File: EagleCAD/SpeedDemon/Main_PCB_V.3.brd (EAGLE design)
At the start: 77 x 46.5 mm, 65 parts, among them Q1 DMC2700, U3 LM3676, U4 STM32F072-LQFP48, X1 32.768kHz

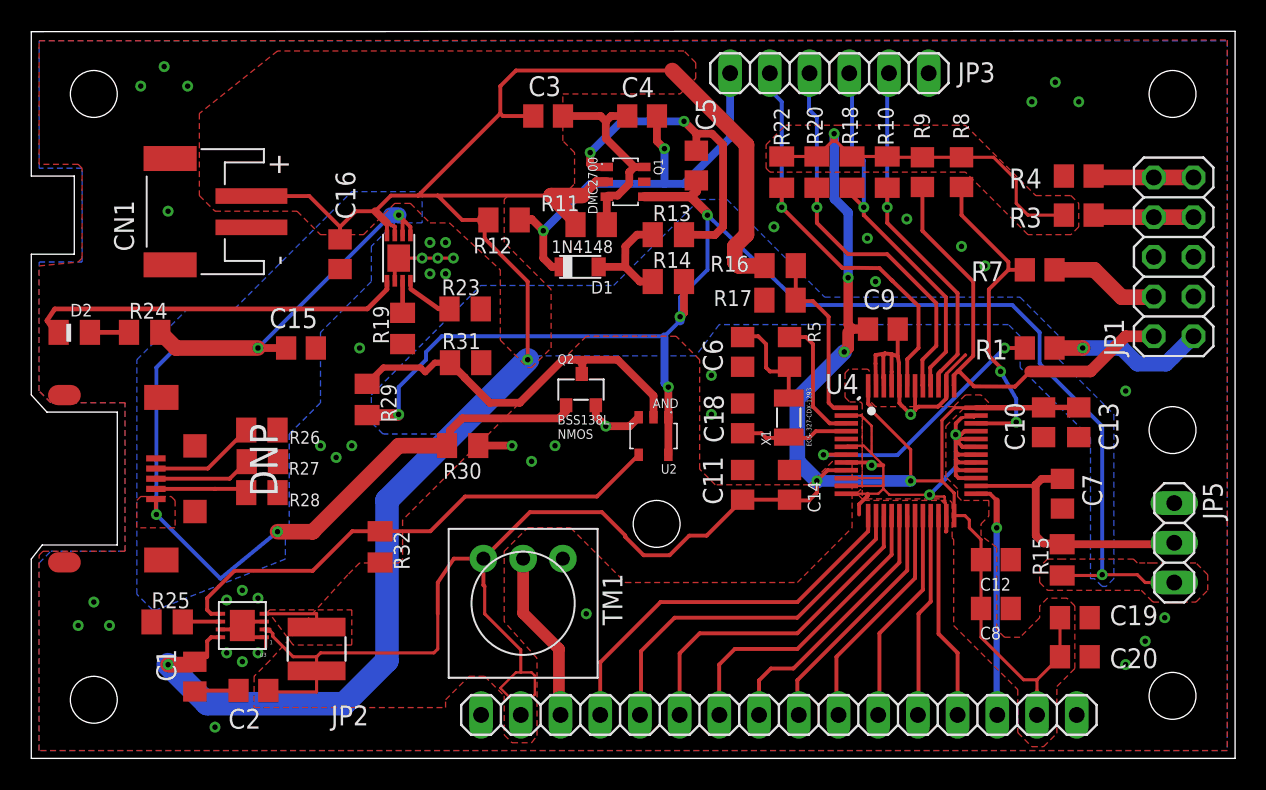
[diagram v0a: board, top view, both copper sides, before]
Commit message: Fixed several DRC errors
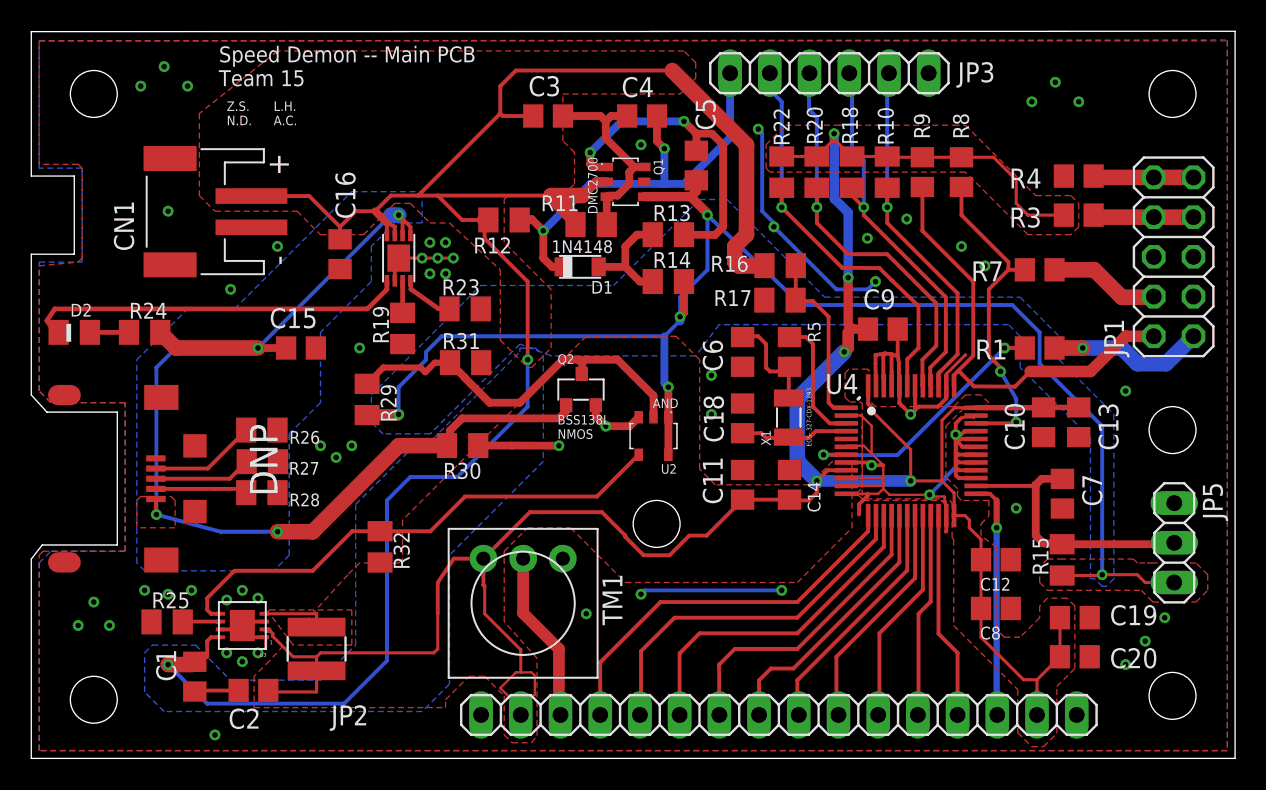
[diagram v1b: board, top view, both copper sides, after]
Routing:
- net GND: track 85.2 -> 112.3 mm, vias 49 -> 57
- net +V+_CHG: track 74.4 -> 71.8 mm
- net VBATT+: track 128.1 -> 129.9 mm
- added copper zone on layer 16, net VBATT+
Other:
- board text added: "L.H. A.C."
- board text added: "Speed Demon -- Main PCB Team 15"
- board text added: "Z.S. N.D."
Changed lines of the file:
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@@
 <setting verticaltext="up"/>
 </settings>
-<grid distance="0.5" unitdist="mm" unit="mm" style="lines" multiple="1" display="no" altdistance="0.01" altunitdist="mm" altunit="mm"/>
+<grid distance="0.25" unitdist="mm" unit="mm" style="lines" multiple="1" display="no" altdistance="0.01" altunitdist="mm" altunit="mm"/>
 <layers>
 <layer number="1" name="Top" color="4" fill="1" visible="yes" active="yes"/>
@@
 <dimension x1="78" y1="46.5" x2="78" y2="42.5" x3="78.5" y3="44.5" textsize="1.778" layer="51"/>
 <dimension x1="77" y1="0" x2="77" y2="21" x3="80" y3="10.5" textsize="1.778" layer="51"/>
+<text x="12" y="43" size="1.016" layer="21">Speed Demon -- Main PCB
+Team 15</text>
+<text x="12.5" y="40.5" size="0.6096" layer="21">Z.S.
+N.D.</text>
+<text x="15.5" y="40.5" size="0.6096" layer="21">L.H.
+A.C.</text>
 </plain>
 <attributes>
@@
 <wire x1="36.11" y1="21.89" x2="36.11" y2="22.59" width="0.5" layer="1"/>
 <via x="36.75" y="21.25" extent="1-16" drill="0.35"/>
-<via x="30.75" y="20" extent="1-16" drill="0.35"/>
+<via x="33.75" y="20" extent="1-16" drill="0.35"/>
 <wire x1="28.59" y1="20.01" x2="30.74" y2="20.01" width="0.5" layer="1"/>
-<wire x1="30.74" y1="20.01" x2="30.75" y2="20" width="0.5" layer="1"/>
+<wire x1="30.74" y1="20.01" x2="33.75" y2="20" width="0.5" layer="1"/>
 <wire x1="52.13" y1="17.93" x2="54.43" y2="17.93" width="0.1524" layer="1"/>
 <wire x1="54.43" y1="17.93" x2="54.5" y2="18" width="0.1524" layer="1"/>
@@
 <via x="8.5" y="44.25" extent="1-16" drill="0.35"/>
 <via x="8.75" y="35" extent="1-16" drill="0.35"/>
-<via x="11.75" y="2" extent="1-16" drill="0.35"/>
+<via x="11.75" y="1.5" extent="1-16" drill="0.35"/>
 <via x="14.5" y="10.25" extent="1-16" drill="0.35"/>
 <wire x1="23.5" y1="32" x2="25" y2="32" width="0.2" layer="1"/>
@@
 <via x="64" y="42" extent="1-16" drill="0.35"/>
 <via x="67" y="42" extent="1-16" drill="0.35"/>
-<via x="32" y="19" extent="1-16" drill="0.35"/>
-<via x="33.5" y="20" extent="1-16" drill="0.35"/>
 <via x="20.5" y="20" extent="1-16" drill="0.35"/>
 <via x="18.5" y="20" extent="1-16" drill="0.35"/>
@@
 <via x="53.48" y="33.27" extent="1-16" drill="0.35"/>
 <via x="70" y="23.5" extent="1-16" drill="0.35"/>
-<wire x1="58.53" y1="14.53" x2="62.65" y2="12.71" width="0" layer="19" extent="1-1"/>
-<wire x1="39.21" y1="36.88" x2="47.5" y2="34" width="0" layer="19" extent="1-1"/>
+<via x="8.75" y="10.5" extent="1-16" drill="0.35"/>
+<via x="10.25" y="10.75" extent="1-16" drill="0.35"/>
+<via x="7.25" y="10.75" extent="1-16" drill="0.35"/>
+<via x="12.75" y="30" extent="1-16" drill="0.35"/>
+<via x="15.75" y="32.75" extent="1-16" drill="0.35"/>
+<via x="39" y="10.5" extent="1-16" drill="0.35"/>
+<via x="48" y="10.75" extent="1-16" drill="0.35"/>
+<wire x1="39" y1="10.5" x2="39.25" y2="10.75" width="0.25" layer="16"/>
+<wire x1="39.25" y1="10.75" x2="48" y2="10.75" width="0.25" layer="16"/>
+<via x="63" y="16" extent="1-16" drill="0.35"/>
+<via x="46.5" y="40.25" extent="1-16" drill="0.35"/>
+<wire x1="46.5" y1="40.25" x2="46.75" y2="40" width="0.25" layer="16"/>
+<wire x1="46.75" y1="35" x2="47.5" y2="34.25" width="0.25" layer="16"/>
+<wire x1="47.5" y1="34.25" x2="47.5" y2="34" width="0.25" layer="16"/>
+<wire x1="46.75" y1="40" x2="46.75" y2="35" width="0.25" layer="16"/>
+<wire x1="47.5" y1="34" x2="51.5" y2="30" width="0.25" layer="16"/>
+<wire x1="51.5" y1="30" x2="53.5" y2="30" width="0.25" layer="16"/>
+<wire x1="53.5" y1="30" x2="54" y2="30.5" width="0.25" layer="16"/>
+<via x="39" y="39.25" extent="1-16" drill="0.35"/>
 </signal>
 <signal name="N$10">
@@
 <vertex x="44" y="27.75"/>
 <vertex x="42.5" y="25.75"/>
-<vertex x="32.5" y="25.75"/>
-<vertex x="28.75" y="21.75"/>
-<vertex x="27.75" y="20.75"/>
+<vertex x="33.25" y="25.75"/>
+<vertex x="31.25" y="26.5"/>
+<vertex x="25.5" y="20.75"/>
 <vertex x="22.5" y="20.75"/>
 <vertex x="21.75" y="21.5"/>
@@
 <contactref element="C15" pad="1"/>
 <via x="8" y="15.6" extent="1-16" drill="0.35"/>
-<wire x1="12.1" y1="11.5" x2="8" y2="15.6" width="0.25" layer="16"/>
-<wire x1="12.1" y1="11.5" x2="15.75" y2="14.5" width="0.25" layer="16"/>
+<wire x1="12.1" y1="14.5" x2="8" y2="15.6" width="0.25" layer="16"/>
+<wire x1="12.1" y1="14.5" x2="15.75" y2="14.5" width="0.25" layer="16"/>
 <wire x1="8" y1="25" x2="9.25" y2="26.25" width="0.25" layer="16"/>
 <wire x1="8" y1="15.6" x2="8" y2="25" width="0.25" layer="16"/>
@@
 <wire x1="9.25" y1="26.25" x2="14.5" y2="26.25" width="1" layer="1"/>
 <polygon width="0.25" layer="16">
-<vertex x="16.25" y="14"/>
-<vertex x="16.25" y="12.75"/>
-<vertex x="8" y="9.5"/>
-<vertex x="7.75" y="9.5"/>
-<vertex x="6.75" y="10.5"/>
+<vertex x="16.5" y="20.75"/>
+<vertex x="16.5" y="13"/>
+<vertex x="15.5" y="12"/>
+<vertex x="7.25" y="12"/>
+<vertex x="6.75" y="12.5"/>
 <vertex x="6.75" y="25.5"/>
 <vertex x="10" y="28.75"/>
@@
 <vertex x="18.5" y="27.25"/>
 <vertex x="18.5" y="22.75"/>
-<vertex x="16.5" y="20.75"/>
-<vertex x="16.5" y="14.25"/>
 </polygon>
 <wire x1="26.59" y1="20.01" x2="26.7376" y2="20.4576" width="0.5" layer="1"/>
@@
 <wire x1="11.25" y1="7.5" x2="11.5" y2="7.75" width="0.25" layer="1"/>
 <wire x1="11.5" y1="7.75" x2="12.1" y2="7.75" width="0.25" layer="1"/>
-<wire x1="31.75" y1="25.5" x2="22.75" y2="16.5" width="1.5" layer="16"/>
-<wire x1="22.75" y1="16.5" x2="22.75" y2="6.25" width="1.5" layer="16"/>
-<wire x1="22.75" y1="6.25" x2="20" y2="3.5" width="1.5" layer="16"/>
+<wire x1="31.75" y1="25.5" x2="31.75" y2="22.5" width="0.25" layer="16"/>
+<wire x1="31.75" y1="22.5" x2="27.25" y2="18" width="0.25" layer="16"/>
+<wire x1="27.25" y1="18" x2="24.25" y2="18" width="0.25" layer="16"/>
+<wire x1="24.25" y1="18" x2="22.75" y2="16.5" width="0.25" layer="16"/>
+<wire x1="22.75" y1="16.5" x2="22.75" y2="6.25" width="0.25" layer="16"/>
+<wire x1="22.75" y1="6.25" x2="20" y2="3.5" width="0.25" layer="16"/>
 <via x="8.75" y="6" extent="1-16" drill="0.35"/>
-<wire x1="20" y1="3.5" x2="11.25" y2="3.5" width="1.5" layer="16"/>
-<wire x1="11.25" y1="3.5" x2="8.75" y2="6" width="1.5" layer="16"/>
+<wire x1="20" y1="3.5" x2="11.25" y2="3.5" width="0.25" layer="16"/>
+<wire x1="11.25" y1="3.5" x2="8.75" y2="6" width="0.25" layer="16"/>
 <wire x1="8.75" y1="6" x2="10.28" y2="6" width="1" layer="1"/>
 <wire x1="10.28" y1="6" x2="10.46" y2="6.18" width="0.25" layer="1"/>
@@
 <vertex x="10.75" y="41.25"/>
 </polygon>
-</signal>
+<polygon width="0.25" layer="16" rank="2">
+<vertex x="31.25" y="26.25"/>
+<vertex x="32.25" y="26.25"/>
+<vertex x="32.75" y="25.75"/>
+<vertex x="32.75" y="19"/>
+<vertex x="26.75" y="13"/>
+<vertex x="26.75" y="4.75"/>
+<vertex x="25" y="3"/>
+<vertex x="8.5" y="3"/>
+<vertex x="7.25" y="4.25"/>
+<vertex x="7.25" y="6.75"/>
+<vertex x="7.75" y="7.25"/>
+<vertex x="10.5" y="7.25"/>
+<vertex x="12.75" y="5"/>
+<vertex x="18.5" y="5"/>
+<vertex x="20.75" y="7.25"/>
+<vertex x="20.75" y="16.25"/>
+<vertex x="24.5" y="20"/>
+<vertex x="25.25" y="20"/>
+<vertex x="31.25" y="26"/>
+</polygon>
+</signal>

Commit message: board revisions, potential switch cap datasheet
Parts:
- moved TM1 3.01 mm to (31.7, 12.9), turned to 90 degrees
- moved U2 1.77 mm to (39.5, 22.4)
- moved R32 0.75 mm to (21.6, 13.5)
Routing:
- net +3V3: track 169.5 -> 163.8 mm
- net N$28: track 24.7 -> 22.9 mm
- net BATT_CHG_LOGIC_OP: track 33.1 -> 34.7 mm
- net GND: track 112.3 -> 113.4 mm
- net VBATT+_SW: track 96.0 -> 95.0 mm
- net N$14: track 11.0 -> 11.7 mm

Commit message: a
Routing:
- net GND: vias 57 -> 56
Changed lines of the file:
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@@
 <layer number="14" name="Route14" color="1" fill="6" visible="no" active="yes"/>
 <layer number="15" name="Route15" color="4" fill="6" visible="no" active="yes"/>
-<layer number="16" name="Bottom" color="1" fill="1" visible="no" active="yes"/>
+<layer number="16" name="Bottom" color="1" fill="1" visible="yes" active="yes"/>
 <layer number="17" name="Pads" color="2" fill="1" visible="yes" active="yes"/>
 <layer number="18" name="Vias" color="2" fill="1" visible="yes" active="yes"/>
@@
 <wire x1="52.95" y1="16.25" x2="52.95" y2="15.6" width="0.25" layer="1"/>
 <via x="65.5" y="43.25" extent="1-16" drill="0.35"/>
-<via x="35.5" y="9.25" extent="1-16" drill="0.35"/>
 <via x="71.25" y="7.5" extent="1-16" drill="0.35"/>
 <via x="25.5" y="33" extent="1-16" drill="0.35"/>
